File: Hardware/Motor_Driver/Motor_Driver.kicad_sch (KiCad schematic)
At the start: 30 parts

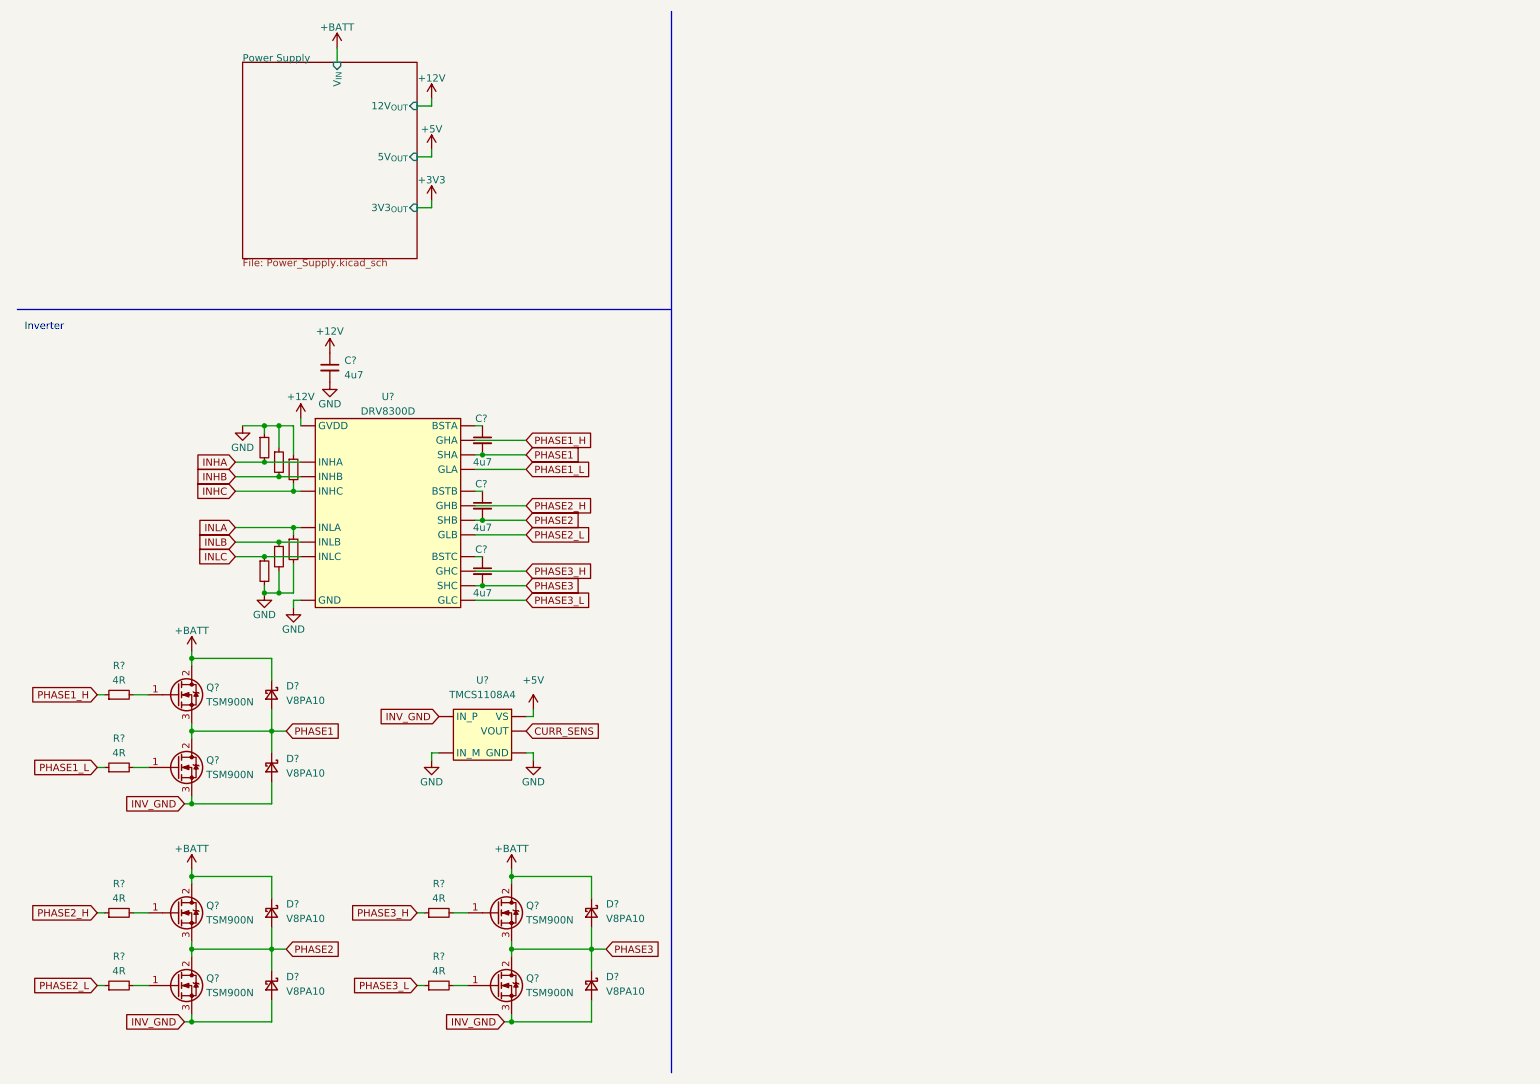
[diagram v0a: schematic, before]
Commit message: Updated hardware design.
Dedicated board for powering the drive motor.
Almost finished the schematic design.
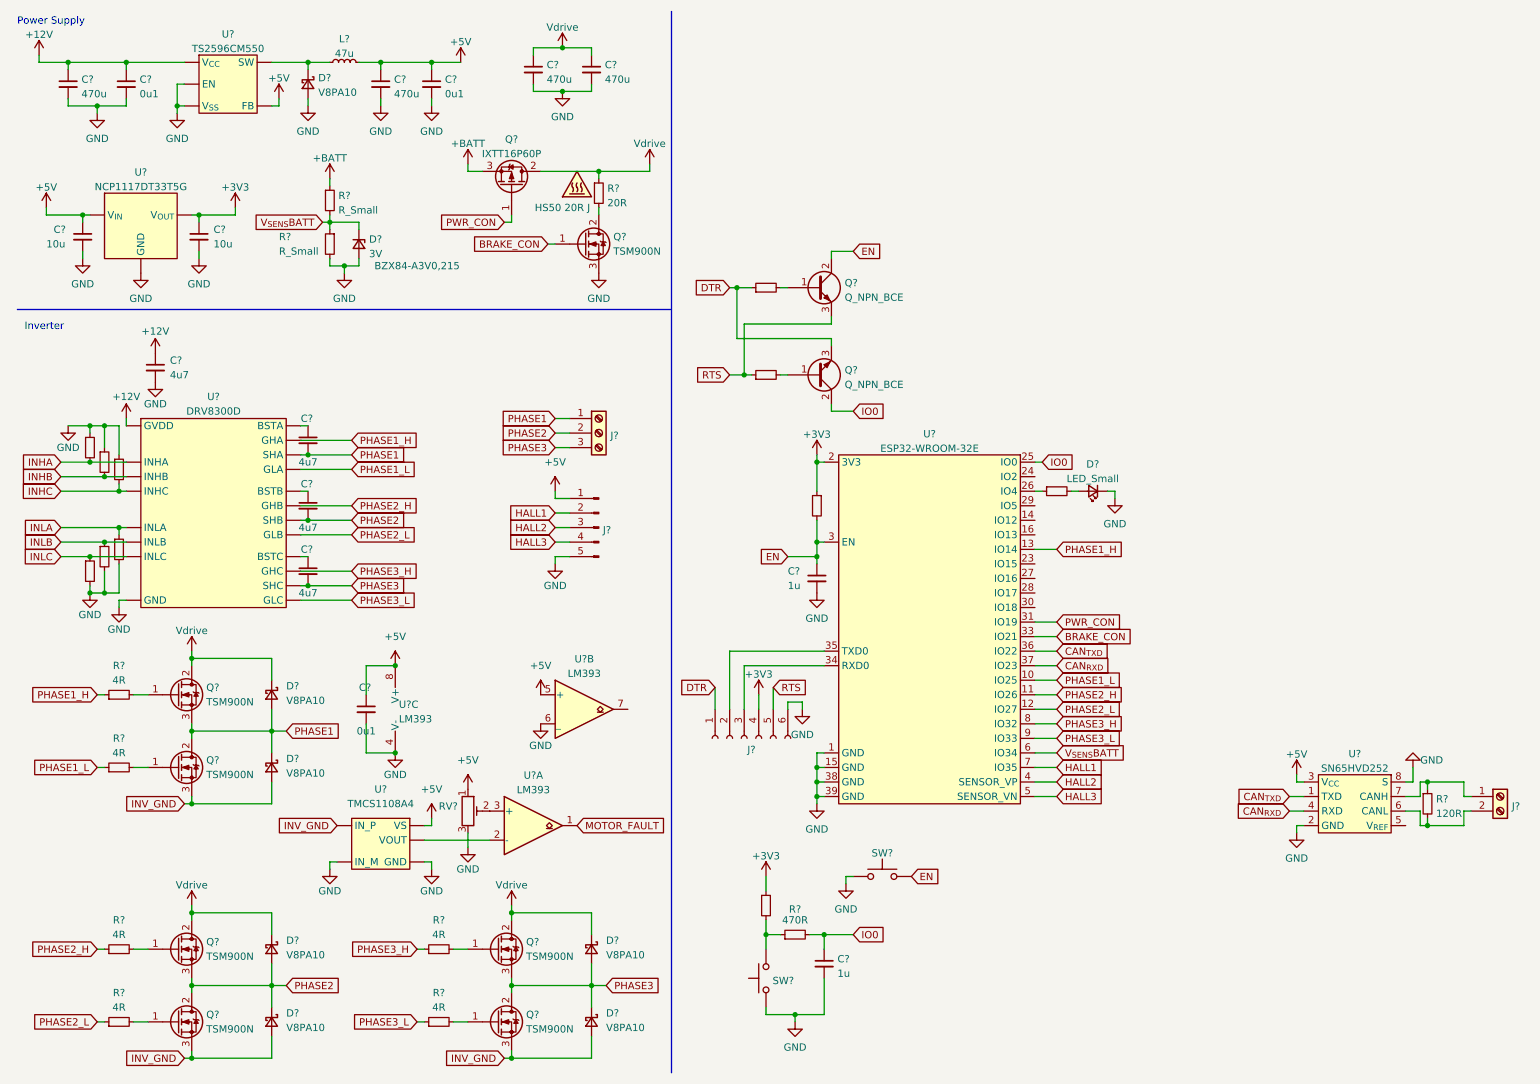
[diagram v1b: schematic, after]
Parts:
- added C? (x2): 10u, symbol Device:C_Small
- added C? (x3): 0u1, symbol Device:C_Small
- added C? (x4): 470u, symbol Device:C_Small
- added C? (x2): 1u, symbol Device:C_Small
- added D?: LED_Small, symbol Device:LED_Small
- added D?: 3V, symbol Device:D_Zener_Small
- added D?: V8PA10, symbol Device:D_Schottky_Small
- added J?: Screw_Terminal_01x02, symbol Connector:Screw_Terminal_01x02
- added J?: Conn_01x05_Male, symbol Connector:Conn_01x05_Male
- added J?: Conn_01x06_Female, symbol Connector:Conn_01x06_Female
- added J?: Screw_Terminal_01x03, symbol Connector:Screw_Terminal_01x03
- added L?: 47u, symbol Device:L_Small
- added Q? (x2): Q_NPN_BCE, symbol Device:Q_NPN_BCE
- added Q?: TSM900N, symbol Device:Q_NMOS_GDS
- added Q?: IXTT16P60P, symbol Device:Q_PMOS_GDS
- added R? (x2): R_Small, symbol Device:R_Small
- added R? (x5): 10k, symbol Device:R_Small
- added R?: 20R, symbol Device:R_Small
- added R?: 120R, symbol Device:R_Small
- added R?: 470R, symbol Device:R_Small
- added RV?: R_Potentiometer_Trim, symbol Device:R_Potentiometer_Trim
- added SW? (x2): SW_Push, symbol Switch:SW_Push
- added U? (x3): LM393, symbol Comparator:LM393
- added U?: NCP1117DT33T5G, symbol Parts_Library:NCP1117
- added U?: ESP32-WROOM-32E, symbol Parts_Library:ESP32-WROOM-32E
- added U?: SN65HVD252, symbol Parts_Library:SN65HVD252
- added U?: TS2596CM550, symbol Parts_Library:TS2596CM550
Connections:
- net +12V: now also C?.1, C?.1, U?.1 (V_{CC})
- net +3V3: now also C?.1, J?.4 (Pin_4), R?.1, R?.1, U?. (V_{OUT}), U?.2 (3V3)
- net +5V: now also C?.1, C?.1, C?.1, C?.1, J?.1 (Pin_1), L?.2, RV?.1, U?. (V_{OUT}), U?.3 (V_{CC}), U?.4 (FB), U?.5 (+), U?.8 (V+)
- net +BATT: now also Q?.3 (S), R?.1; no longer D?.1 (K), D?.1 (K), D?.1 (K), Q?.2 (D), Q?.2 (D), Q?.2 (D)
- net GND: now also C?.2, C?.2, C?.2, C?.2, C?.2, C?.2, C?.2, C?.2, C?.2, C?.2, C?.2, D?.1 (K), D?.2 (A), D?.2 (A), J?.5 (Pin_5), J?.6 (Pin_6), Q?.3 (S), R?.2, RV?.3, SW?.1, SW?.1, U?. (V_{OUT}), U?.1 (GND), U?.15 (GND), U?.2 (GND), U?.3 (V_{SS}), U?.38 (GND), U?.39 (GND), U?.4 (V-), U?.5 (EN), U?.6 (_), U?.8 (S)
- net PHASE1: now also J?.1 (Pin_1)
- net PHASE1_H: now also U?.13 (IO14)
- net PHASE1_L: now also U?.10 (IO25)
- net PHASE2: now also J?.2 (Pin_2)
- net PHASE2_H: now also U?.11 (IO26)
- net PHASE2_L: now also U?.12 (IO27)
- net PHASE3: now also J?.3 (Pin_3)
- net PHASE3_H: now also U?.8 (IO32)
- net PHASE3_L: now also U?.9 (IO33)
- net CURR_SENS: no longer names the net of U?.7 (VOUT)
- net CURR_SENS: now also U?.2 (-)
- new net: Q?.1 (B), R?.2 (x2)
- new net: Q?.2 (D), R?.2
- new net: D?.1 (K), L?.1, U?.2 (SW)
- new net: R?.1, R?.2, SW?.2
- new net: D?.2 (A), R?.2
- new net: RV?.2, U?.3 (+)
- new net: J?.1 (Pin_1), R?.1, U?.7 (CANH)
- new net: J?.2 (Pin_2), R?.2, U?.6 (CANL)
- new net: R?.1, U?.26 (IO4)
- new net: J?.3 (Pin_3), U?.34 (RXD0)
- new net: J?.2 (Pin_2), U?.35 (TXD0)
- new net BRAKE_CON: Q?.1 (G), U?.33 (IO21)
- new net CAN_{RXD}: U?.37 (IO23), U?.4 (RXD)
- new net CAN_{TXD}: U?.1 (TXD), U?.36 (IO22)
- new net DTR: J?.1 (Pin_1), Q?.3 (E), R?.1
- new net EN: C?.1, Q?.2 (C), R?.2, SW?.2, U?.3 (EN)
- new net HALL1: J?.2 (Pin_2), U?.7 (IO35)
- new net HALL2: J?.3 (Pin_3), U?.4 (SENSOR_VP)
- new net HALL3: J?.4 (Pin_4), U?.5 (SENSOR_VN)
- new net IO0: C?.1, Q?.2 (C), R?.2, U?.25 (IO0)
- new net MOTOR_FAULT: U?.1
- new net PWR_CON: Q?.1 (G), U?.31 (IO19)
- new net RTS: J?.5 (Pin_5), Q?.3 (E), R?.1
- new net V_{SENS}BATT: D?.1 (K), R?.1, R?.2, U?.6 (IO34)
- new net Vdrive: C?.1, C?.1, D?.1 (K), D?.1 (K), D?.1 (K), Q?.2 (D), Q?.2 (D), Q?.2 (D), Q?.2 (D), R?.1
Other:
- removed sheet Power Supply
- note added: "Power Supply"
- moved on the sheet: C?, D?, Q?, R?, U?

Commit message: Updated hardware.
Removed battery voltage sensor from driver as the driver can be informed about that information over CAN bus
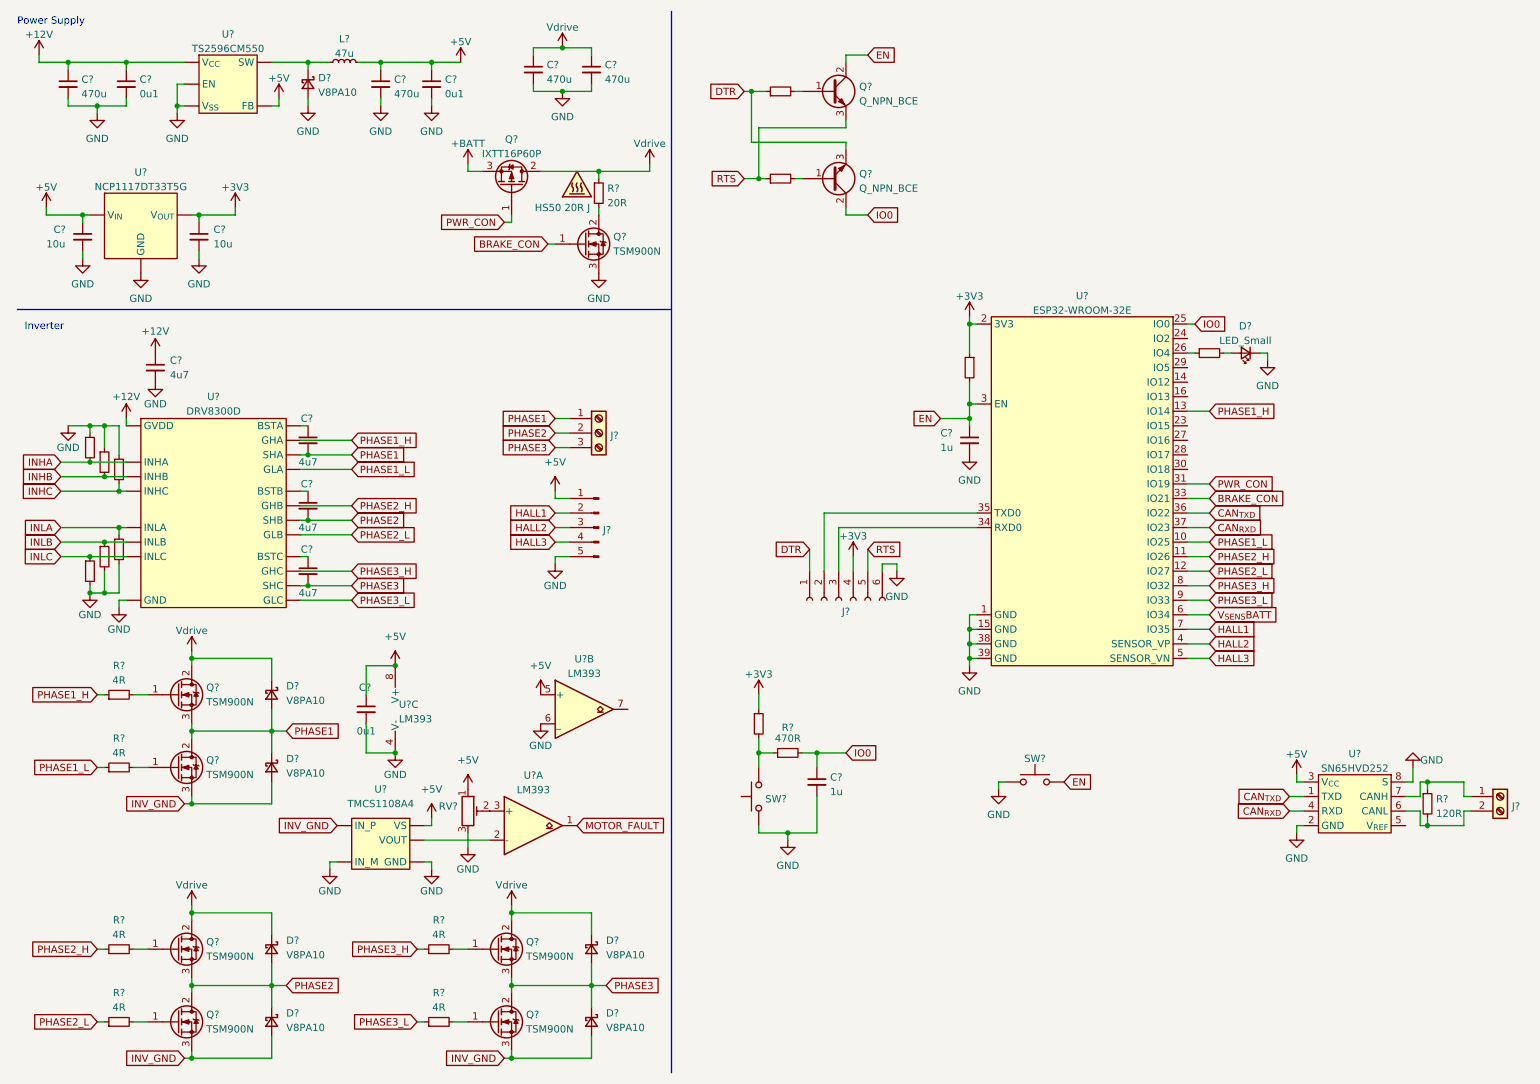
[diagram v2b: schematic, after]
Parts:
- removed D?: 3V, symbol Device:D_Zener_Small
- removed R? (x2): R_Small, symbol Device:R_Small
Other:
- moved on the sheet: C?, D?, J?, Q?, R?, SW?, U?

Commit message: Updated motor driver shematic.
Happy with it now. Time to move on to creating a list of components, sources, prices and footprints.
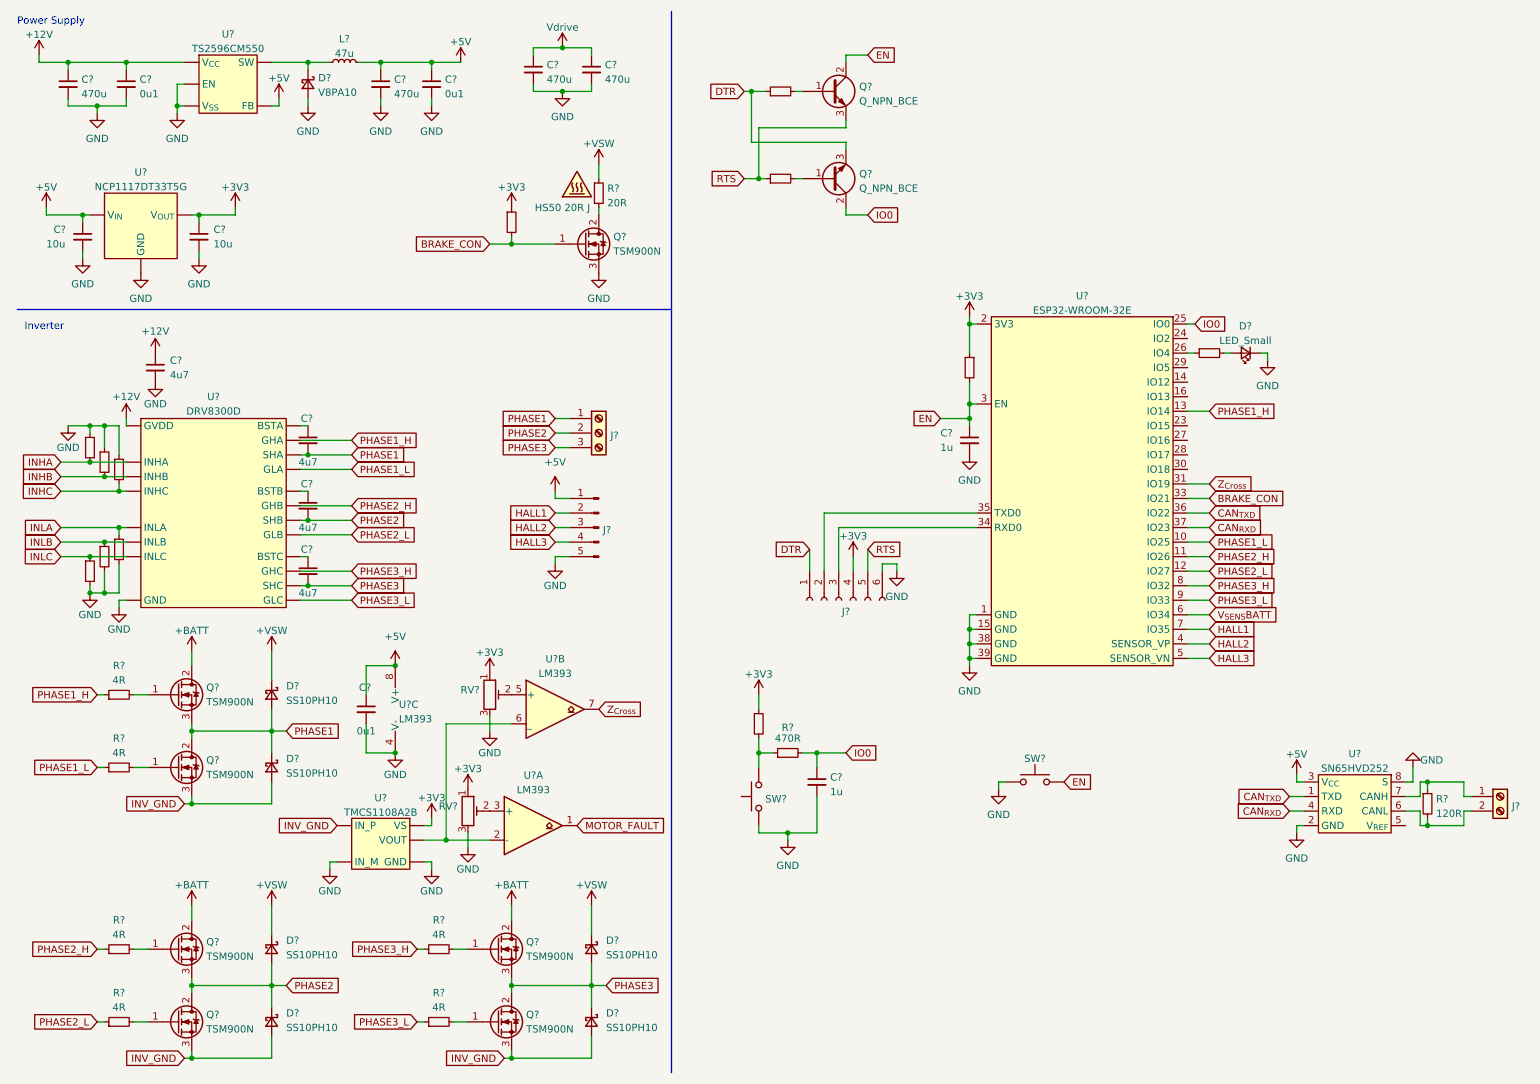
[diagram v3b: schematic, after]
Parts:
- removed Q?: IXTT16P60P, symbol Device:Q_PMOS_GDS
- added R?: 10k, symbol Device:R_Small
- added RV?: R_Potentiometer_Trim, symbol Device:R_Potentiometer_Trim
- D? (x6): value V8PA10 -> SS10PH10
- U?: value TMCS1108A4 -> TMCS1108A2B
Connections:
- net PWR_CON is gone; now on net Z_{Cross}: U?.31 (IO19)
- net +3V3: now also RV?.1, U?.8 (VS), R?.1, RV?.1
- net +5V: no longer RV?.1, U?.5 (+), U?.8 (VS)
- net +BATT: now also Q?.2 (D), Q?.2 (D), Q?.2 (D)
- net BRAKE_CON: now also R?.2
- net GND: now also RV?.3; no longer U?.6 (_)
- net Vdrive: no longer D?.1 (K), D?.1 (K), D?.1 (K), Q?.2 (D), Q?.2 (D), Q?.2 (D), R?.1
- net at U?.2 (-), U?.7 (VOUT): now also U?.6 (_)
- net Z_{Cross}: now reaches U?.7
- new net: RV?.2, U?.5 (+)
- new net +VSW: D?.1 (K), D?.1 (K), D?.1 (K), R?.1
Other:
- moved on the sheet: U?B
